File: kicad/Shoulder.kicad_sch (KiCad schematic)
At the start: 4 parts, among them U301 USBLC6-2SC6

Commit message: One shining moment
Commit board while it still works
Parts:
- added G301, G302: KwanSystems, KwanSystems:StKwansSoldermask, symbol KwanSystems:KwanSystems
- added G303: DesignedWithKicad, KwanSystems:Symbol_KiCAD-Logo_CopperAndSilkScreenTop_small, symbol KwanSystems:DesignedWithKicad
- added G304: OSHW, KwanSystems:OSHW-Symbol_6.7x6mm_SolderMask, symbol KwanSystems:OSHW
- G305: symbol KwanSystems:OSHW -> KwanSystems:Axis
- R301: footprint KwanSystems:R_Array_Convex_2x0402 -> Resistor_SMD:R_0402_1005Metric; symbol KwanSystems:RP2 -> KwanSystems:RESISTOR; Digikey (none) -> CC marker
- R302: renamed from R301; footprint KwanSystems:R_Array_Convex_2x0402 -> Resistor_SMD:R_0402_1005Metric; symbol KwanSystems:RP2 -> KwanSystems:RESISTOR; Digikey (none) -> CC marker
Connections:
- net Q_CC2: now also R302.1; no longer R302.2 (4)
- net Q_GND: now also R301.2, R302.2; no longer R301.4 (3), R302.3
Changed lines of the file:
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@@
     (effects (font (size 1.27 1.27)) (justify right))
   )
-  (symbol (lib_id "KwanSystems:OSHW") (at 262.89 40.64 0) (unit 1)
+  (symbol (lib_id "KwanSystems:Axis") (at 219.71 161.29 0) (unit 1)
     (in_bom yes) (on_board yes)
-    (property "Reference" "G305" (id 0) (at 262.89 43.18 0)
+    (property "Reference" "G305" (id 0) (at 228.6 161.29 0)
+      (effects (font (size 1.524 1.524)))
+    )
+    (property "Value" "Axis" (id 1) (at 214.63 160.02 0)
+      (effects (font (size 1.524 1.524)) (justify left) hide)
+    )
+    (property "Footprint" "KwanSystems:Axis" (id 2) (at 219.71 161.29 0)
+      (effects (font (size 1.27 1.27)) hide)
+    )
+    (property "Datasheet" "" (id 3) (at 219.71 161.29 0)
+      (effects (font (size 1.27 1.27)) hide)
+    )
+  )
+  (symbol (lib_id "KwanSystems:DesignedWithKicad") (at 201.93 152.4 0) (unit 1)
+    (in_bom yes) (on_board yes)
+    (property "Reference" "G303" (id 0) (at 213.36 152.4 0)
+      (effects (font (size 1.524 1.524)))
+    )
+    (property "Value" "DesignedWithKicad" (id 1) (at 203.2 152.4 0)
+      (effects (font (size 1.524 1.524)) (justify left) hide)
+    )
+    (property "Footprint" "KwanSystems:Symbol_KiCAD-Logo_CopperAndSilkScreenTop_small" (id 2) (at 201.93 152.4 0)
       (effects (font (size 1.524 1.524)) hide)
     )
-    (property "Value" "Axis" (id 1) (at 257.81 38.1 0)
-      (effects (font (size 1.524 1.524)) (justify left))
-    )
-    (property "Footprint" "KwanSystems:Axis" (id 2) (at 262.89 40.64 0)
+    (property "Datasheet" "" (id 3) (at 201.93 152.4 0)
       (effects (font (size 1.524 1.524)) hide)
     )
-    (property "Datasheet" "" (id 3) (at 262.89 40.64 0)
+  )
+  (symbol (lib_name "KwanSystems_1") (lib_id "KwanSystems:KwanSystems") (at 181.61 152.4 0) (unit 1)
+    (in_bom yes) (on_board yes)
+    (property "Reference" "G301" (id 0) (at 190.5 152.4 0)
+      (effects (font (size 1.524 1.524)))
+    )
+    (property "Value" "KwanSystems" (id 1) (at 182.245 152.4 0)
+      (effects (font (size 1.524 1.524)) (justify left) hide)
+    )
+    (property "Footprint" "KwanSystems:StKwansSoldermask" (id 2) (at 181.61 152.4 0)
+      (effects (font (size 1.524 1.524)) hide)
+    )
+    (property "Datasheet" "" (id 3) (at 181.61 152.4 0)
       (effects (font (size 1.524 1.524)) hide)
     )
@@
     (pin "2")
   )
-  (symbol (lib_id "KwanSystems:RP2") (at 158.75 93.98 0) (unit 2)
+  (symbol (lib_id "KwanSystems:RESISTOR") (at 158.75 93.98 0) (unit 1)
     (in_bom yes) (on_board yes)
-    (property "Reference" "R301" (id 0) (at 153.67 92.71 0)
+    (property "Reference" "R302" (id 0) (at 153.67 92.71 0)
       (effects (font (size 1.143 1.143)))
     )
@@
       (effects (font (size 1.143 1.143)))
     )
-    (property "Footprint" "KwanSystems:R_Array_Convex_2x0402" (id 2) (at 160.147 90.17 0)
+    (property "Footprint" "Resistor_SMD:R_0402_1005Metric" (id 2) (at 160.147 90.17 0)
       (effects (font (size 0.508 0.508)) hide)
     )
@@
       (effects (font (size 1.27 1.27)) hide)
     )
+    (property "Digikey" "CC marker" (id 5) (at 158.75 93.98 0)
+      (effects (font (size 1.27 1.27)) hide)
+    )
+    (pin "1")
     (pin "2")
-    (pin "3")
   )
   (symbol (lib_id "Power_Protection:USBLC6-2SC6") (at 180.34 35.56 270) (mirror x) (unit 1)
@@
     (pin "6")
   )
-  (symbol (lib_id "KwanSystems:RP2") (at 158.75 91.44 0) (unit 1)
+  (symbol (lib_id "KwanSystems:KwanSystems") (at 181.61 161.29 0) (unit 1)
+    (in_bom yes) (on_board yes)
+    (property "Reference" "G302" (id 0) (at 190.5 161.29 0)
+      (effects (font (size 1.524 1.524)))
+    )
+    (property "Value" "KwanSystems" (id 1) (at 182.245 161.29 0)
+      (effects (font (size 1.524 1.524)) (justify left) hide)
+    )
+    (property "Footprint" "KwanSystems:StKwansSoldermask" (id 2) (at 181.61 161.29 0)
+      (effects (font (size 1.524 1.524)) hide)
+    )
+    (property "Datasheet" "" (id 3) (at 181.61 161.29 0)
+      (effects (font (size 1.524 1.524)) hide)
+    )
+  )
+  (symbol (lib_id "KwanSystems:RESISTOR") (at 158.75 91.44 0) (unit 1)
     (in_bom yes) (on_board yes)
     (property "Reference" "R301" (id 0) (at 153.67 90.17 0)
@@
       (effects (font (size 1.143 1.143)))
     )
-    (property "Footprint" "KwanSystems:R_Array_Convex_2x0402" (id 2) (at 160.147 87.63 0)
+    (property "Footprint" "Resistor_SMD:R_0402_1005Metric" (id 2) (at 160.147 87.63 0)
       (effects (font (size 0.508 0.508)) hide)
     )
@@
       (effects (font (size 1.27 1.27)) hide)
     )
+    (property "Digikey" "CC marker" (id 5) (at 158.75 91.44 0)
+      (effects (font (size 1.27 1.27)) hide)
+    )
     (pin "1")
-    (pin "4")
+    (pin "2")
+  )
+  (symbol (lib_id "KwanSystems:OSHW") (at 200.66 161.29 0) (unit 1)
+    (in_bom yes) (on_board yes)
+    (property "Reference" "G304" (id 0) (at 213.36 161.29 0)
+      (effects (font (size 1.524 1.524)))
+    )
+    (property "Value" "OSHW" (id 1) (at 201.295 161.29 0)
+      (effects (font (size 1.524 1.524)) (justify left) hide)
+    )
+    (property "Footprint" "KwanSystems:OSHW-Symbol_6.7x6mm_SolderMask" (id 2) (at 200.66 161.29 0)
+      (effects (font (size 1.524 1.524)) hide)
+    )
+    (property "Datasheet" "" (id 3) (at 200.66 161.29 0)
+      (effects (font (size 1.524 1.524)) hide)
+    )
   )
   (sheet (at 38.1 163.83) (size 25.4 15.24) (fields_autoplaced)

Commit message: Updated graphical elements
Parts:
- G301, G302, G303, G304, G305: now left out of the parts list
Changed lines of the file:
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@@
   )
   (symbol (lib_id "KwanSystems:Axis") (at 219.71 161.29 0) (unit 1)
-    (in_bom yes) (on_board yes)
+    (in_bom no) (on_board yes)
     (property "Reference" "G305" (id 0) (at 228.6 161.29 0)
       (effects (font (size 1.524 1.524)))
@@
   )
   (symbol (lib_id "KwanSystems:DesignedWithKicad") (at 201.93 152.4 0) (unit 1)
-    (in_bom yes) (on_board yes)
+    (in_bom no) (on_board yes)
     (property "Reference" "G303" (id 0) (at 213.36 152.4 0)
       (effects (font (size 1.524 1.524)))
@@
     )
   )
-  (symbol (lib_name "KwanSystems_1") (lib_id "KwanSystems:KwanSystems") (at 181.61 152.4 0) (unit 1)
-    (in_bom yes) (on_board yes)
+  (symbol (lib_id "KwanSystems:KwanSystems") (at 181.61 152.4 0) (unit 1)
+    (in_bom no) (on_board yes)
     (property "Reference" "G301" (id 0) (at 190.5 152.4 0)
       (effects (font (size 1.524 1.524)))
@@
   )
   (symbol (lib_id "KwanSystems:KwanSystems") (at 181.61 161.29 0) (unit 1)
-    (in_bom yes) (on_board yes)
+    (in_bom no) (on_board yes)
     (property "Reference" "G302" (id 0) (at 190.5 161.29 0)
       (effects (font (size 1.524 1.524)))
@@
   )
   (symbol (lib_id "KwanSystems:OSHW") (at 200.66 161.29 0) (unit 1)
-    (in_bom yes) (on_board yes)
+    (in_bom no) (on_board yes)
     (property "Reference" "G304" (id 0) (at 213.36 161.29 0)
       (effects (font (size 1.524 1.524)))

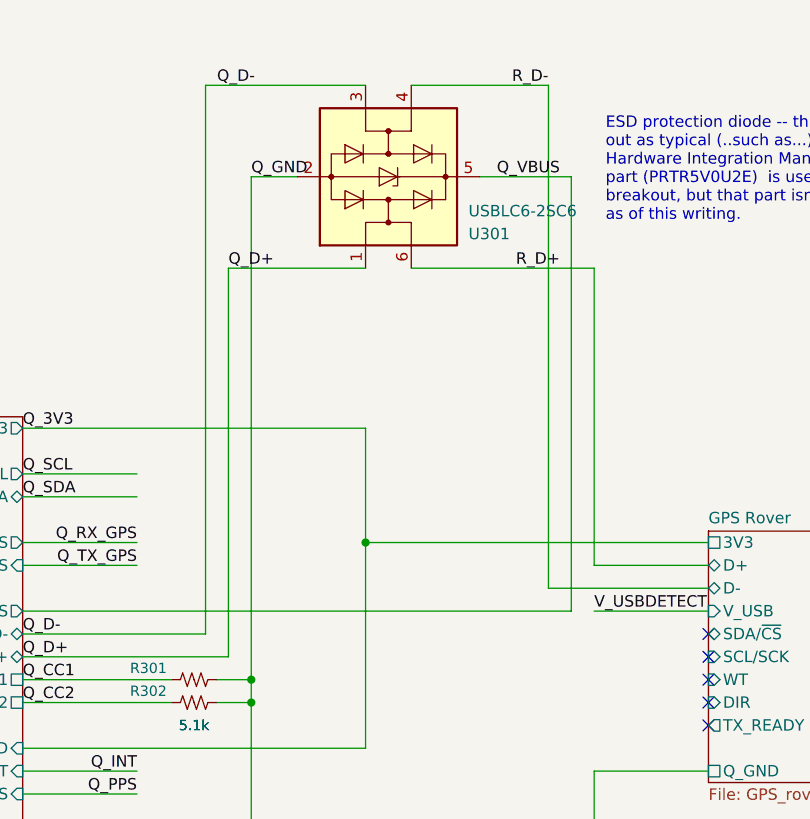
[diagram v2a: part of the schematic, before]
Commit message: Changed protection diode for USB lines
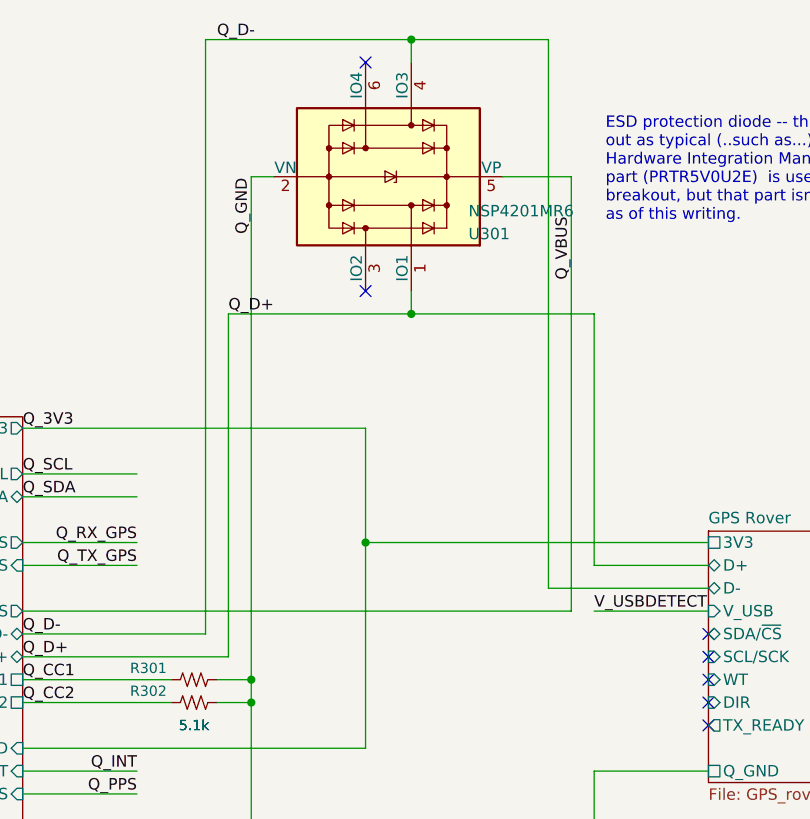
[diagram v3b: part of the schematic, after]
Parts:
- U301: value USBLC6-2SC6 -> NSP4201MR6; symbol Power_Protection:USBLC6-2SC6 -> Power_Protection:SRV05-4
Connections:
- net R_D- is gone; now on net Q_D-: U301.4 (IO3)
- net Q_D-: no longer U301.3 (I/O2)
- net R_D+: no longer names the net of U301.6 (IO4)
- no-connect marks 14 -> 16
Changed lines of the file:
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@@
   (junction (at 177.8 76.2) (diameter 0) (color 0 0 0 0)
   )
+  (junction (at 182.88 20.32) (diameter 0) (color 0 0 0 0)
+  )
   (junction (at 165.1 93.98) (diameter 0) (color 0 0 0 0)
   )
+  (junction (at 182.88 50.8) (diameter 0) (color 0 0 0 0)
+  )
   (junction (at 35.56 165.1) (diameter 0) (color 0 0 0 0)
   )
@@
   )
   (no_connect (at 215.9 96.52))
+  (no_connect (at 177.8 22.86))
   (no_connect (at 139.7 109.22))
+  (no_connect (at 177.8 48.26))
   (no_connect (at 215.9 93.98))
   (no_connect (at 215.9 91.44))
@@
     (stroke (width 0) (type default) (color 0 0 0 0))
   )
-  (wire (pts (xy 160.02 25.4) (xy 177.8 25.4))
-    (stroke (width 0) (type default) (color 0 0 0 0))
-  )
   (wire (pts (xy 165.1 91.44) (xy 165.1 93.98))
     (stroke (width 0) (type default) (color 0 0 0 0))
@@
     (stroke (width 0) (type default) (color 0 0 0 0))
   )
-  (wire (pts (xy 170.18 35.56) (xy 165.1 35.56))
+  (wire (pts (xy 167.64 35.56) (xy 165.1 35.56))
     (stroke (width 0) (type default) (color 0 0 0 0))
   )
@@
     (stroke (width 0) (type default) (color 0 0 0 0))
   )
+  (wire (pts (xy 182.88 50.8) (xy 182.88 48.26))
+    (stroke (width 0) (type default) (color 0 0 0 0))
+  )
   (wire (pts (xy 101.6 101.6) (xy 110.49 101.6))
     (stroke (width 0) (type default) (color 0 0 0 0))
@@
     (stroke (width 0) (type default) (color 0 0 0 0))
   )
-  (wire (pts (xy 198.12 81.28) (xy 198.12 25.4))
+  (wire (pts (xy 198.12 81.28) (xy 198.12 20.32))
+    (stroke (width 0) (type default) (color 0 0 0 0))
+  )
+  (wire (pts (xy 160.02 20.32) (xy 182.88 20.32))
     (stroke (width 0) (type default) (color 0 0 0 0))
   )
@@
     (stroke (width 0) (type default) (color 0 0 0 0))
   )
-  (wire (pts (xy 182.88 25.4) (xy 198.12 25.4))
+  (wire (pts (xy 182.88 20.32) (xy 198.12 20.32))
     (stroke (width 0) (type default) (color 0 0 0 0))
   )
@@
     (stroke (width 0) (type default) (color 0 0 0 0))
   )
-  (wire (pts (xy 162.56 88.9) (xy 162.56 45.72))
+  (wire (pts (xy 162.56 88.9) (xy 162.56 50.8))
     (stroke (width 0) (type default) (color 0 0 0 0))
   )
@@
     (stroke (width 0) (type default) (color 0 0 0 0))
   )
-  (wire (pts (xy 160.02 86.36) (xy 160.02 25.4))
-    (stroke (width 0) (type default) (color 0 0 0 0))
-  )
-  (wire (pts (xy 203.2 45.72) (xy 203.2 78.74))
+  (wire (pts (xy 160.02 86.36) (xy 160.02 20.32))
+    (stroke (width 0) (type default) (color 0 0 0 0))
+  )
+  (wire (pts (xy 203.2 50.8) (xy 203.2 78.74))
     (stroke (width 0) (type default) (color 0 0 0 0))
   )
@@
     (stroke (width 0) (type default) (color 0 0 0 0))
   )
-  (wire (pts (xy 177.8 45.72) (xy 162.56 45.72))
-    (stroke (width 0) (type default) (color 0 0 0 0))
-  )
-  (wire (pts (xy 182.88 45.72) (xy 203.2 45.72))
+  (wire (pts (xy 182.88 50.8) (xy 203.2 50.8))
     (stroke (width 0) (type default) (color 0 0 0 0))
   )
@@
     (stroke (width 0) (type default) (color 0 0 0 0))
   )
-  (wire (pts (xy 190.5 35.56) (xy 200.66 35.56))
+  (wire (pts (xy 193.04 35.56) (xy 200.66 35.56))
     (stroke (width 0) (type default) (color 0 0 0 0))
   )
@@
     (stroke (width 0) (type default) (color 0 0 0 0))
   )
+  (wire (pts (xy 182.88 20.32) (xy 182.88 22.86))
+    (stroke (width 0) (type default) (color 0 0 0 0))
+  )
   (wire (pts (xy 139.7 78.74) (xy 152.4 78.74))
     (stroke (width 0) (type default) (color 0 0 0 0))
@@
   )
   (wire (pts (xy 101.6 78.74) (xy 110.49 78.74))
+    (stroke (width 0) (type default) (color 0 0 0 0))
+  )
+  (wire (pts (xy 162.56 50.8) (xy 182.88 50.8))
     (stroke (width 0) (type default) (color 0 0 0 0))
   )
@@
     (effects (font (size 1.27 1.27)) (justify left bottom))
   )
-  (label "Q_D+" (at 162.56 45.72 0)
+  (label "Q_D+" (at 162.56 50.8 0)
     (effects (font (size 1.27 1.27)) (justify left bottom))
   )
@@
     (effects (font (size 1.27 1.27)) (justify left bottom))
   )
-  (label "R_D+" (at 199.39 45.72 180)
-    (effects (font (size 1.27 1.27)) (justify right bottom))
-  )
   (label "Q_SCL" (at 76.2 129.54 180)
     (effects (font (size 1.27 1.27)) (justify right bottom))
   )
-  (label "Q_GND" (at 165.1 35.56 0)
-    (effects (font (size 1.27 1.27)) (justify left bottom))
-  )
-  (label "Q_VBUS" (at 199.39 35.56 180)
-    (effects (font (size 1.27 1.27)) (justify right bottom))
+  (label "Q_GND" (at 165.1 41.91 90)
+    (effects (font (size 1.27 1.27)) (justify left bottom))
+  )
+  (label "Q_VBUS" (at 200.66 46.99 90)
+    (effects (font (size 1.27 1.27)) (justify left bottom))
   )
   (label "Q_INT" (at 76.2 132.08 180)
@@
     (effects (font (size 1.27 1.27)) (justify left bottom))
   )
-  (label "R_D-" (at 198.12 25.4 180)
-    (effects (font (size 1.27 1.27)) (justify right bottom))
-  )
-  (label "Q_D-" (at 161.29 25.4 0)
+  (label "Q_D-" (at 161.29 20.32 0)
     (effects (font (size 1.27 1.27)) (justify left bottom))
   )
@@
     (pin "2")
   )
-  (symbol (lib_id "Power_Protection:USBLC6-2SC6") (at 180.34 35.56 270) (mirror x) (unit 1)
+  (symbol (lib_id "Power_Protection:SRV05-4") (at 180.34 35.56 270) (mirror x) (unit 1)
     (in_bom yes) (on_board yes)
     (property "Reference" "U301" (id 0) (at 189.23 41.91 90)
       (effects (font (size 1.27 1.27)) (justify left))
     )
-    (property "Value" "USBLC6-2SC6" (id 1) (at 189.23 39.37 90)
+    (property "Value" "NSP4201MR6" (id 1) (at 189.23 39.37 90)
       (effects (font (size 1.27 1.27)) (justify left))
     )
-    (property "Footprint" "Package_TO_SOT_SMD:SOT-23-6" (id 2) (at 167.64 35.56 0)
-      (effects (font (size 1.27 1.27)) hide)
-    )
-    (property "Datasheet" "https://www.st.com/resource/en/datasheet/usblc6-2.pdf" (id 3) (at 189.23 30.48 0)
-      (effects (font (size 1.27 1.27)) hide)
-    )
+    (property "Footprint" "Package_TO_SOT_SMD:SOT-23-6" (id 2) (at 168.91 17.78 0)
+      (effects (font (size 1.27 1.27)) hide)
+    )
+    (property "Datasheet" "http://www.onsemi.com/pub/Collateral/SRV05-4-D.PDF" (id 3) (at 180.34 35.56 0)
+      (effects (font (size 1.27 1.27)) hide)
+    )

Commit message: Updated Digikey part number
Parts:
- R301, R302: Digikey CC marker -> P5.1KJCT-ND
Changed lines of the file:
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@@
       (effects (font (size 1.27 1.27)) hide)
     )
-    (property "Digikey" "CC marker" (id 5) (at 158.75 93.98 0)
+    (property "Digikey" "P5.1KJCT-ND" (id 5) (at 158.75 93.98 0)
       (effects (font (size 1.27 1.27)) hide)
     )
@@
       (effects (font (size 1.27 1.27)) hide)
     )
-    (property "Digikey" "CC marker" (id 5) (at 158.75 91.44 0)
+    (property "Digikey" "P5.1KJCT-ND" (id 5) (at 158.75 91.44 0)
       (effects (font (size 1.27 1.27)) hide)
     )
